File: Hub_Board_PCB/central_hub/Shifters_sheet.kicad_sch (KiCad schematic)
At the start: 15 parts, among them Q1 BSS138, Q2 BSS138, Q3 BSS138, Q4 BSS138, Q5 BSS138

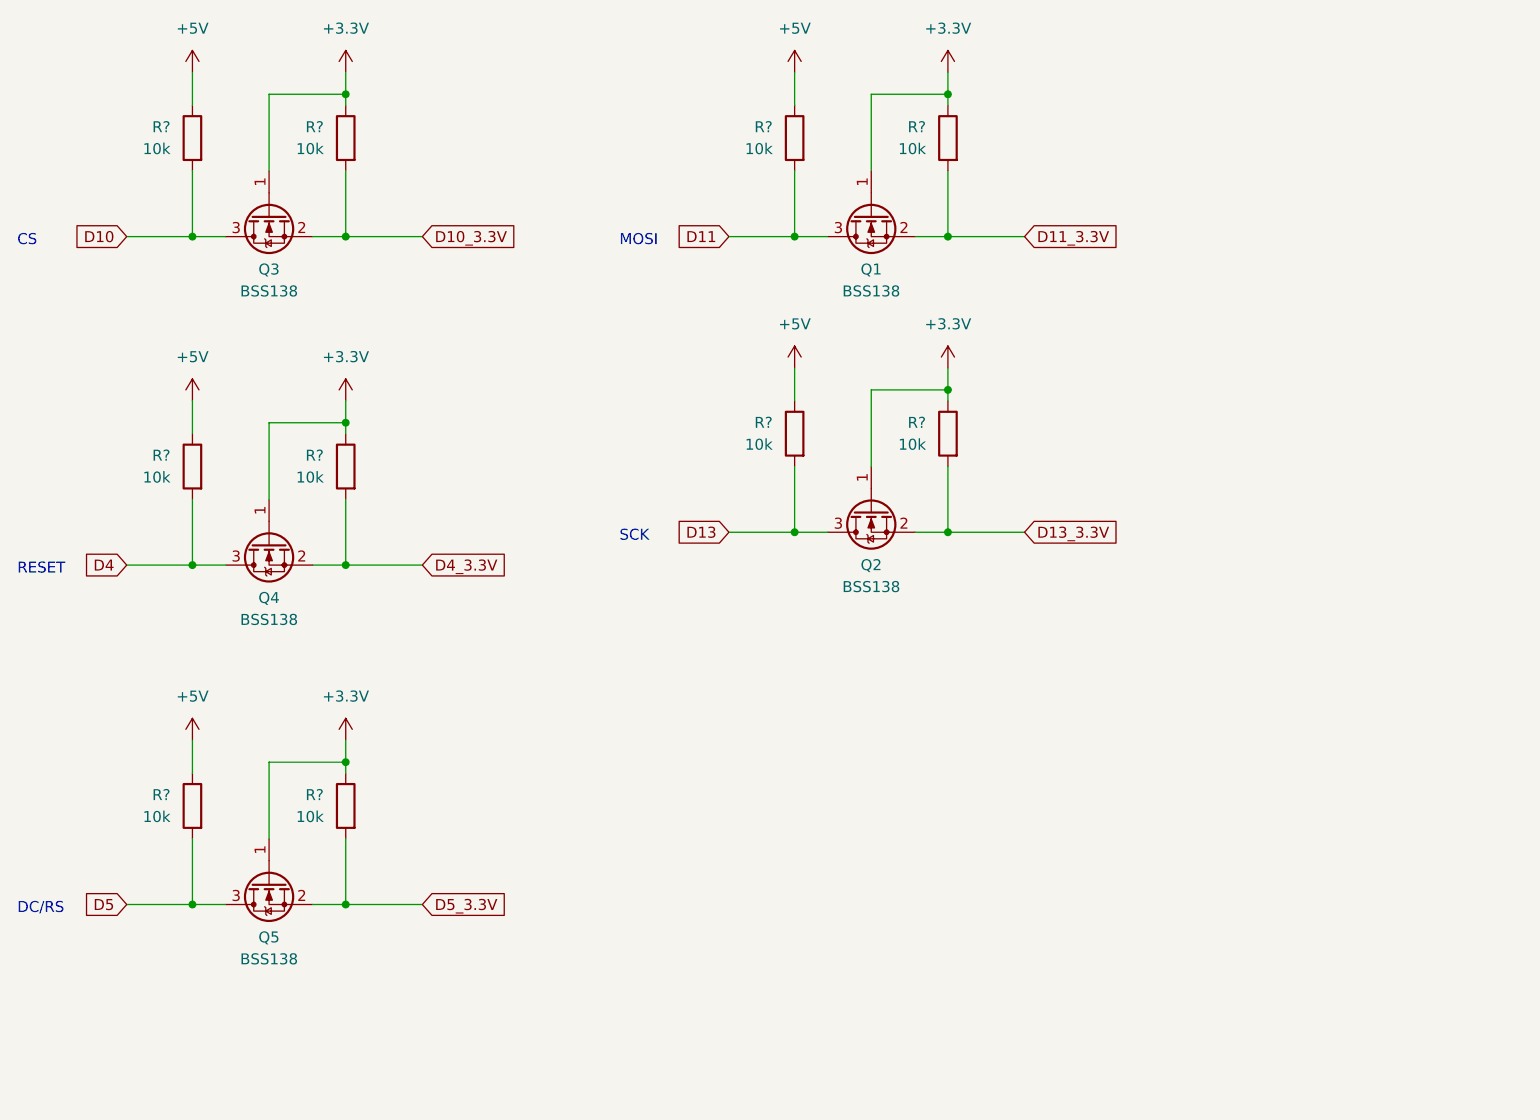
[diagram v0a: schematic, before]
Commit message: - fixed capacitor values on MCU sheet (both central hub and motor board) - added missing Accelerometer componenets - changed BOOT HEADER (both central hub and motor board) - set the Arduino "love" signal to NC - fixed overlapping pins on USB connector
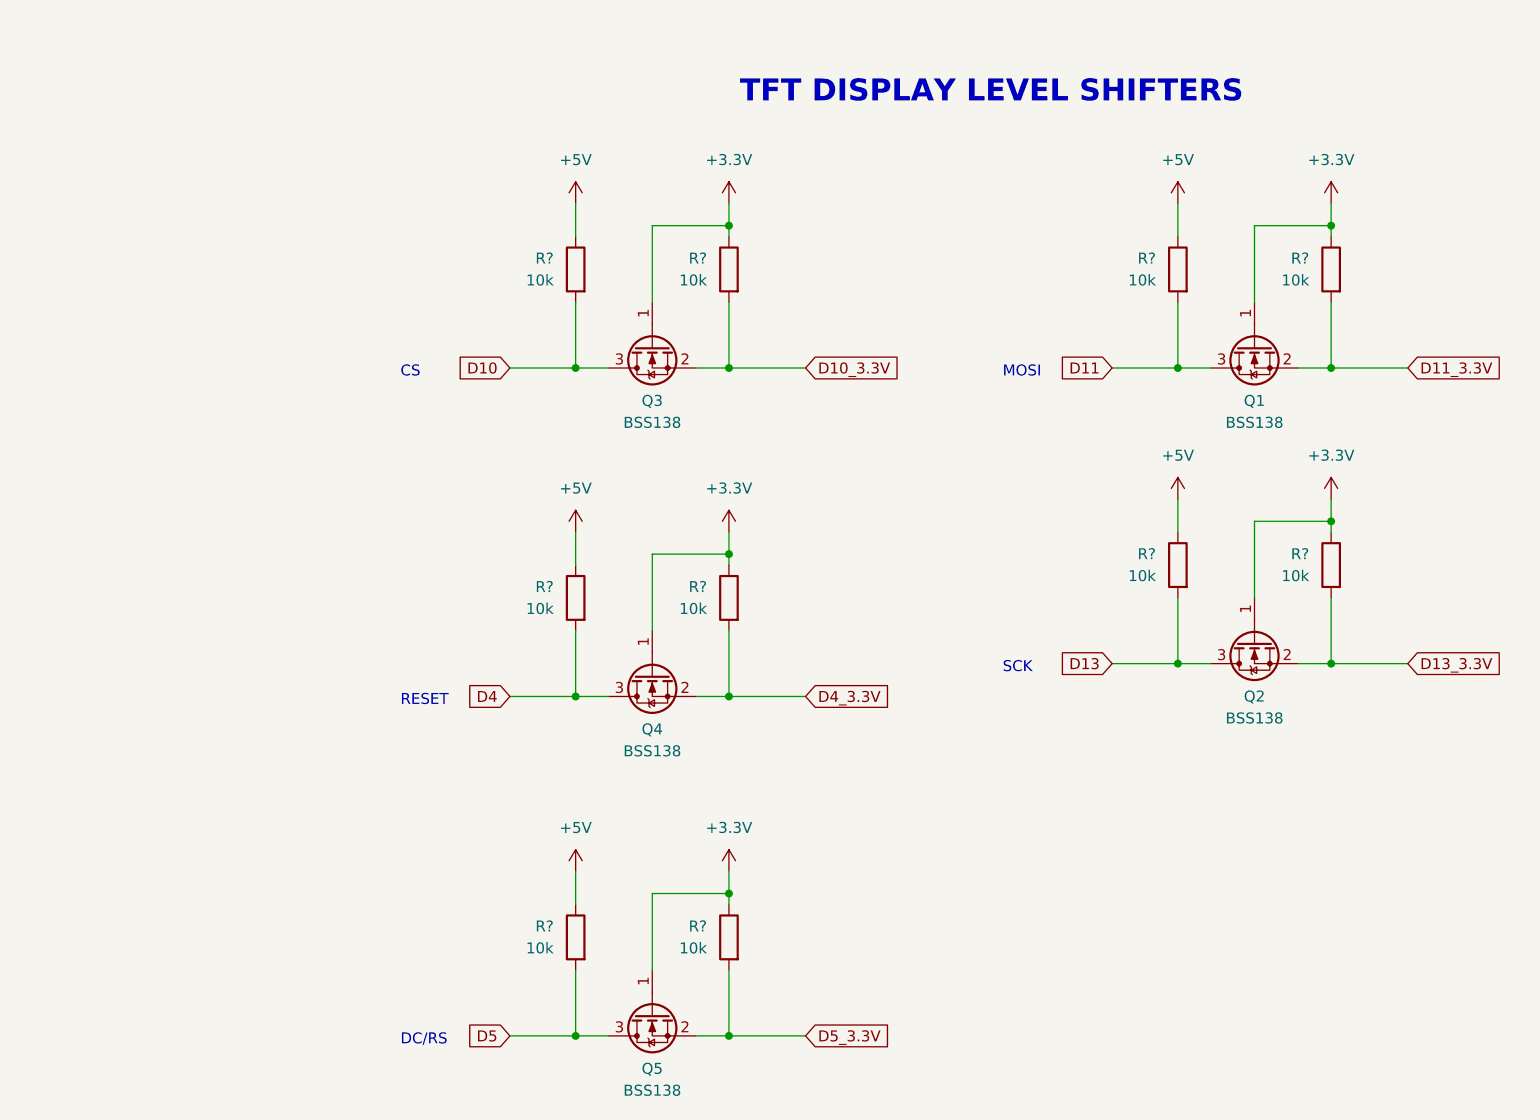
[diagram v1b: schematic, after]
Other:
- note added: "TFT DISPLAY LEVEL SHIFTERS"
- moved on the sheet: Q1, Q2, Q3, Q4, Q5, R?

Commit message: - added footprint labels to schematic
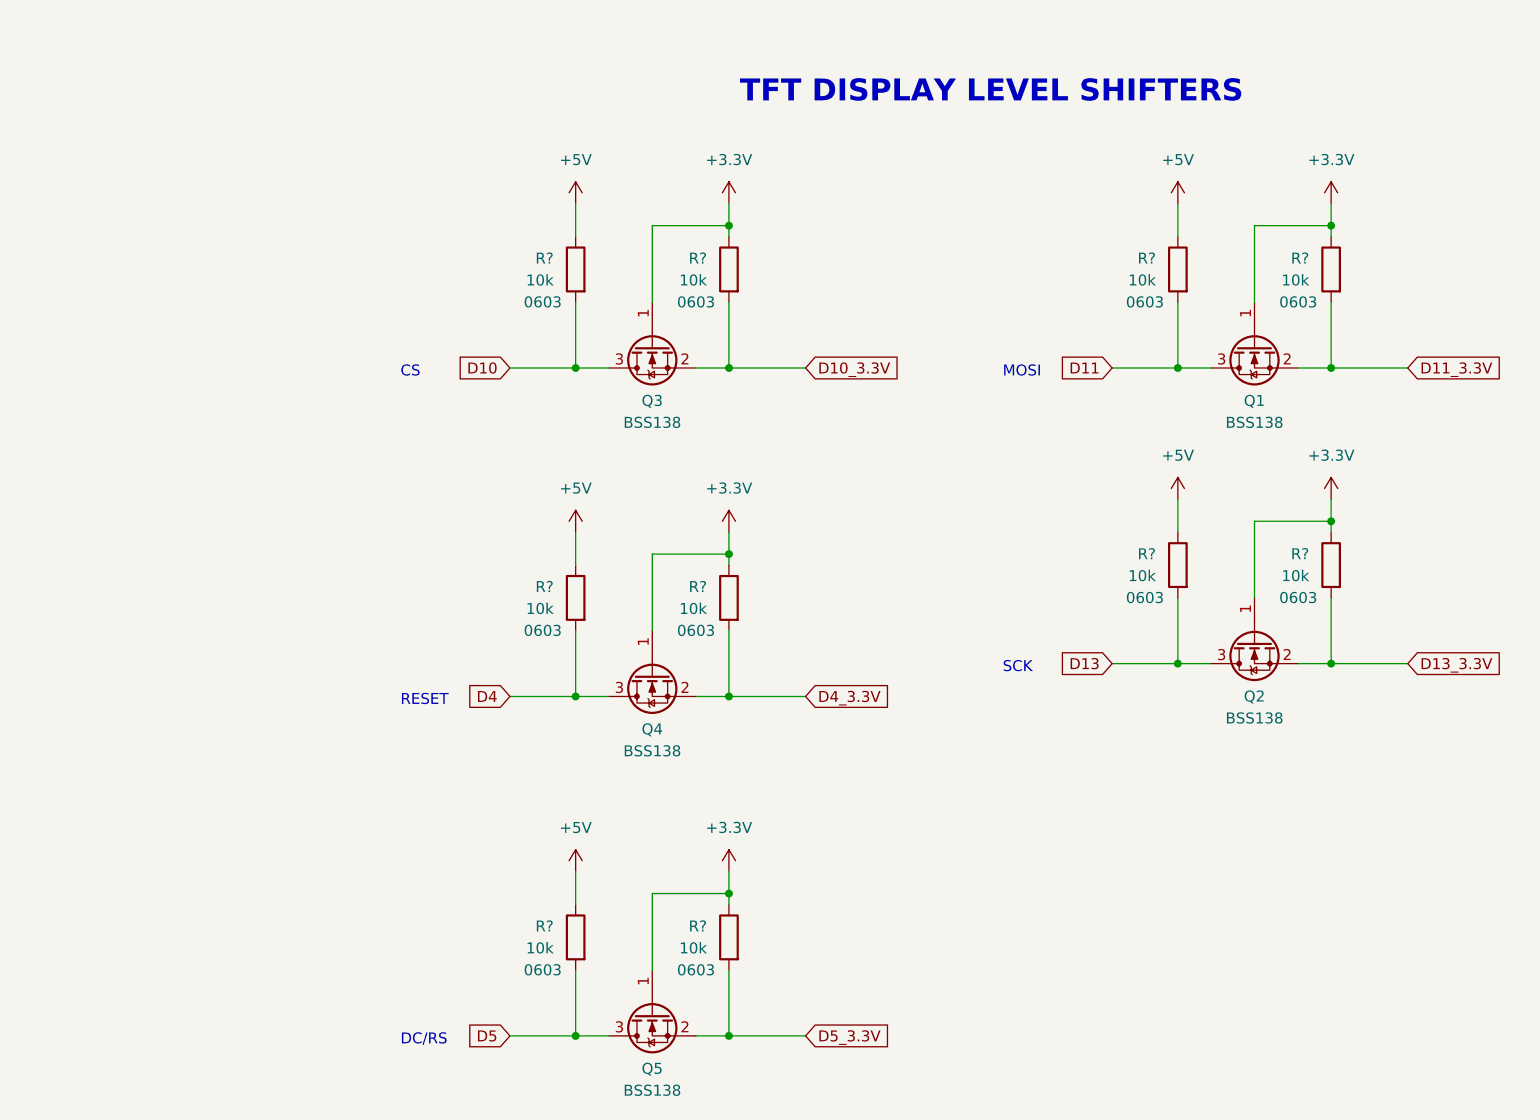
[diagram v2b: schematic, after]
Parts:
- R? (x10): FP (none) -> 0603
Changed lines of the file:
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@@
   )
   (symbol (lib_id "Device:R") (at 124.46 58.42 0) (mirror y) (unit 1)
-    (in_bom yes) (on_board yes) (dnp no) (fields_autoplaced)
+    (in_bom yes) (on_board yes) (dnp no)
     (property "Reference" "R?" (at 121.92 57.15 0)
       (effects (font (size 1.27 1.27)) (justify left))
@@
     (property "Datasheet" "~" (at 124.46 58.42 0)
       (effects (font (size 1.27 1.27)) hide)
+    )
+    (property "FP" "0603" (at 120.65 62.23 0)
+      (effects (font (size 1.27 1.27)))
     )
     (pin "1")
@@
   )
   (symbol (lib_id "Device:R") (at 106.68 135.89 0) (mirror y) (unit 1)
-    (in_bom yes) (on_board yes) (dnp no) (fields_autoplaced)
+    (in_bom yes) (on_board yes) (dnp no)
     (property "Reference" "R?" (at 104.14 134.62 0)
       (effects (font (size 1.27 1.27)) (justify left))
@@
     (property "Datasheet" "~" (at 106.68 135.89 0)
       (effects (font (size 1.27 1.27)) hide)
+    )
+    (property "FP" "0603" (at 102.87 139.7 0)
+      (effects (font (size 1.27 1.27)))
     )
     (pin "1")
@@
   )
   (symbol (lib_id "Device:R") (at 124.46 135.89 0) (mirror y) (unit 1)
-    (in_bom yes) (on_board yes) (dnp no) (fields_autoplaced)
+    (in_bom yes) (on_board yes) (dnp no)
     (property "Reference" "R?" (at 121.92 134.62 0)
       (effects (font (size 1.27 1.27)) (justify left))
@@
     (property "Datasheet" "~" (at 124.46 135.89 0)
       (effects (font (size 1.27 1.27)) hide)
+    )
+    (property "FP" "0603" (at 120.65 139.7 0)
+      (effects (font (size 1.27 1.27)))
     )
     (pin "1")
@@
   )
   (symbol (lib_id "Device:R") (at 106.68 96.52 0) (mirror y) (unit 1)
-    (in_bom yes) (on_board yes) (dnp no) (fields_autoplaced)
+    (in_bom yes) (on_board yes) (dnp no)
     (property "Reference" "R?" (at 104.14 95.25 0)
       (effects (font (size 1.27 1.27)) (justify left))
@@
     (property "Datasheet" "~" (at 106.68 96.52 0)
       (effects (font (size 1.27 1.27)) hide)
+    )
+    (property "FP" "0603" (at 102.87 100.33 0)
+      (effects (font (size 1.27 1.27)))
     )
     (pin "1")
@@
   )
   (symbol (lib_id "Device:R") (at 194.31 58.42 0) (mirror y) (unit 1)
-    (in_bom yes) (on_board yes) (dnp no) (fields_autoplaced)
+    (in_bom yes) (on_board yes) (dnp no)
     (property "Reference" "R?" (at 191.77 57.15 0)
       (effects (font (size 1.27 1.27)) (justify left))
@@
       (effects (font (size 1.27 1.27)) hide)
     )
+    (property "FP" "0603" (at 190.5 62.23 0)
+      (effects (font (size 1.27 1.27)))
+    )
     (pin "1")
     (pin "2")
@@
   )
   (symbol (lib_id "Device:R") (at 176.53 92.71 0) (mirror y) (unit 1)
-    (in_bom yes) (on_board yes) (dnp no) (fields_autoplaced)
+    (in_bom yes) (on_board yes) (dnp no)
     (property "Reference" "R?" (at 173.99 91.44 0)
       (effects (font (size 1.27 1.27)) (justify left))
@@
       (effects (font (size 1.27 1.27)) hide)
     )
+    (property "FP" "0603" (at 172.72 96.52 0)
+      (effects (font (size 1.27 1.27)))
+    )
     (pin "1")
     (pin "2")
@@
   )
   (symbol (lib_id "Device:R") (at 194.31 92.71 0) (mirror y) (unit 1)
-    (in_bom yes) (on_board yes) (dnp no) (fields_autoplaced)
+    (in_bom yes) (on_board yes) (dnp no)
     (property "Reference" "R?" (at 191.77 91.44 0)
       (effects (font (size 1.27 1.27)) (justify left))
@@
       (effects (font (size 1.27 1.27)) hide)
     )
+    (property "FP" "0603" (at 190.5 96.52 0)
+      (effects (font (size 1.27 1.27)))
+    )
     (pin "1")
     (pin "2")
@@
   )
   (symbol (lib_id "Device:R") (at 176.53 58.42 0) (mirror y) (unit 1)
-    (in_bom yes) (on_board yes) (dnp no) (fields_autoplaced)
+    (in_bom yes) (on_board yes) (dnp no)
     (property "Reference" "R?" (at 173.99 57.15 0)
       (effects (font (size 1.27 1.27)) (justify left))
@@
       (effects (font (size 1.27 1.27)) hide)
     )
+    (property "FP" "0603" (at 172.72 62.23 0)
+      (effects (font (size 1.27 1.27)))
+    )
     (pin "1")
     (pin "2")
@@
   )
   (symbol (lib_id "Device:R") (at 124.46 96.52 0) (mirror y) (unit 1)
-    (in_bom yes) (on_board yes) (dnp no) (fields_autoplaced)
+    (in_bom yes) (on_board yes) (dnp no)
     (property "Reference" "R?" (at 121.92 95.25 0)
       (effects (font (size 1.27 1.27)) (justify left))
@@
       (effects (font (size 1.27 1.27)) hide)
     )
+    (property "FP" "0603" (at 120.65 100.33 0)
+      (effects (font (size 1.27 1.27)))
+    )
     (pin "1")
     (pin "2")
@@
   )
   (symbol (lib_id "Device:R") (at 106.68 58.42 0) (mirror y) (unit 1)
-    (in_bom yes) (on_board yes) (dnp no) (fields_autoplaced)
+    (in_bom yes) (on_board yes) (dnp no)
     (property "Reference" "R?" (at 104.14 57.15 0)
       (effects (font (size 1.27 1.27)) (justify left))
@@
       (effects (font (size 1.27 1.27)) hide)
     )
-    (pin "1")
+    (property "FP" "0603" (at 102.87 62.23 0)
+      (effects (font (size 1.27 1.27)))
+    )
+    (pin "1")
